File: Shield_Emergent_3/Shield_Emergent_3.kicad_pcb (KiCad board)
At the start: 2 copper layers, 23.6 x 33.4 mm, 17 parts, among them J1 USB3_B_Micro, J2 Conn_02x03_Odd_Even, J3 USB3_B_Micro, U3 SP3012-06UTG, U4 SP3012-06UTG, X1 USB_C_24pins

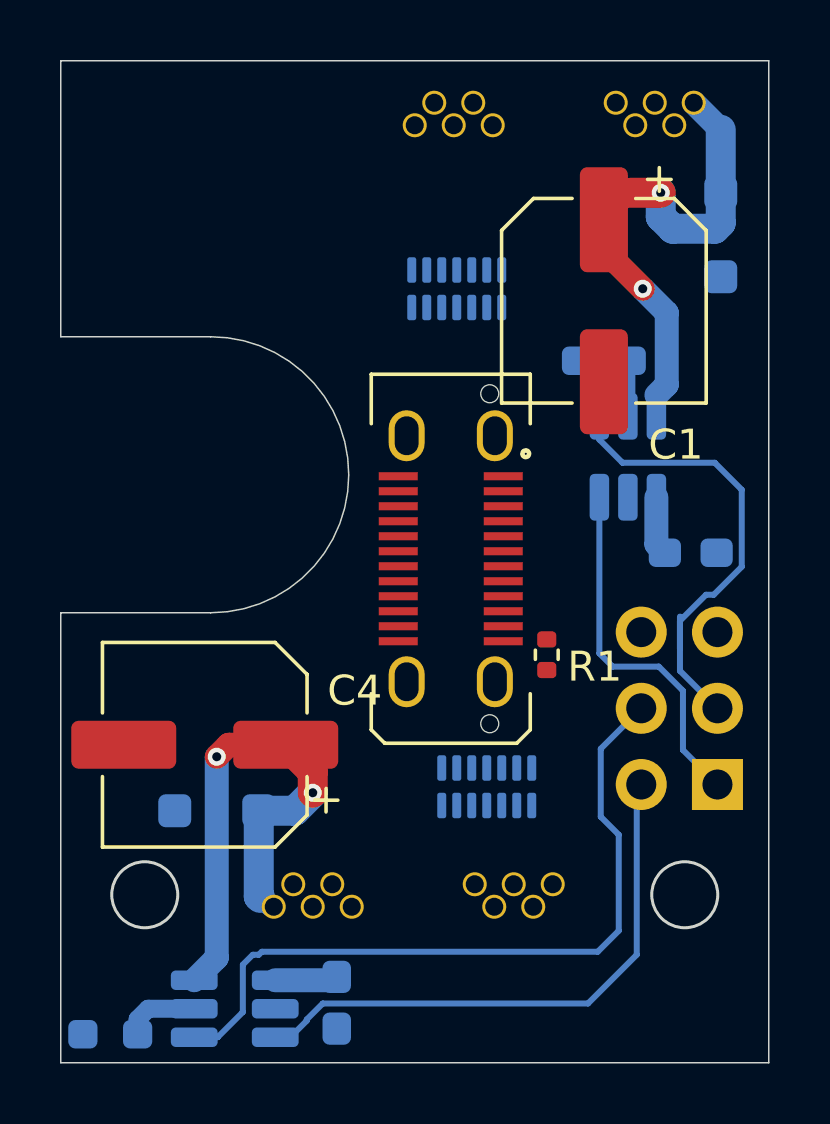
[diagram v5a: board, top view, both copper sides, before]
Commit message: v1.2 internal layers were added
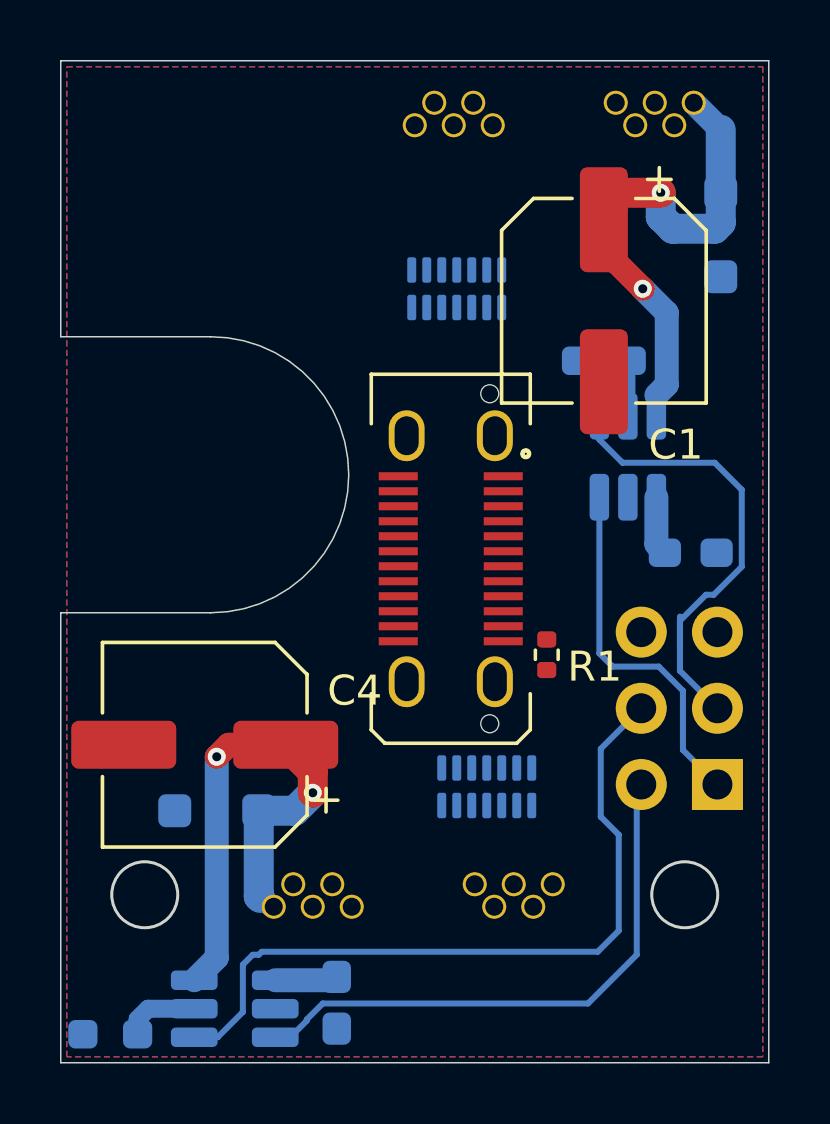
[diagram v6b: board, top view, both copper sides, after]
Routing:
- added copper zone on B.Cu, net GND
- added copper zone on F.Cu, net GND
- added copper zone on In1.Cu, net GND
- added copper zone on In2.Cu, net GND
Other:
- copper layers 2 -> 4
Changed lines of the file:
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@@
 	(layers
 		(0 "F.Cu" signal)
+		(1 "In1.Cu" signal)
+		(2 "In2.Cu" signal)
 		(31 "B.Cu" signal)
 		(32 "B.Adhes" user "B.Adhesive")
@@
 	)
 	(setup
+		(stackup
+			(layer "F.SilkS"
+				(type "Top Silk Screen")
+			)
+			(layer "F.Paste"
+				(type "Top Solder Paste")
+			)
+			(layer "F.Mask"
+				(type "Top Solder Mask")
+				(thickness 0.01)
+			)
+			(layer "F.Cu"
+				(type "copper")
+				(thickness 0.035)
+			)
+			(layer "dielectric 1"
+				(type "prepreg")
+				(thickness 0.1)
+				(material "FR4")
+				(epsilon_r 4.5)
+				(loss_tangent 0.02)
+			)
+			(layer "In1.Cu"
+				(type "copper")
+				(thickness 0.035)
+			)
+			(layer "dielectric 2"
+				(type "core")
+				(thickness 1.24)
+				(material "FR4")
+				(epsilon_r 4.5)
+				(loss_tangent 0.02)
+			)
+			(layer "In2.Cu"
+				(type "copper")
+				(thickness 0.035)
+			)
+			(layer "dielectric 3"
+				(type "prepreg")
+				(thickness 0.1)
+				(material "FR4")
+				(epsilon_r 4.5)
+				(loss_tangent 0.02)
+			)
+			(layer "B.Cu"
+				(type "copper")
+				(thickness 0.035)
+			)
+			(layer "B.Mask"
+				(type "Bottom Solder Mask")
+				(thickness 0.01)
+			)
+			(layer "B.Paste"
+				(type "Bottom Solder Paste")
+			)
+			(layer "B.SilkS"
+				(type "Bottom Silk Screen")
+			)
+			(copper_finish "None")
+			(dielectric_constraints no)
+		)
 		(pad_to_mask_clearance 0)
 		(allow_soldermask_bridges_in_footprints no)
@@
 		(net 27)
 	)
+	(zone
+		(net 2)
+		(net_name "GND")
+		(layers "F.Cu" "In1.Cu" "In2.Cu" "B.Cu")
+		(hatch edge 0.5)
+		(connect_pads
+			(clearance 0.5)
+		)
+		(min_thickness 0.25)
+		(filled_areas_thickness no)
+		(fill yes
+			(thermal_gap 0.5)
+			(thermal_bridge_width 0.5)
+		)
+		(polygon
+			(pts
+				(xy 2.4 0.4) (xy 25.6 0.4) (xy 25.6 33.4) (xy 2.4 33.4)
+			)
+		)
+	)
 )

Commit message: v1.3 draft routing was completed
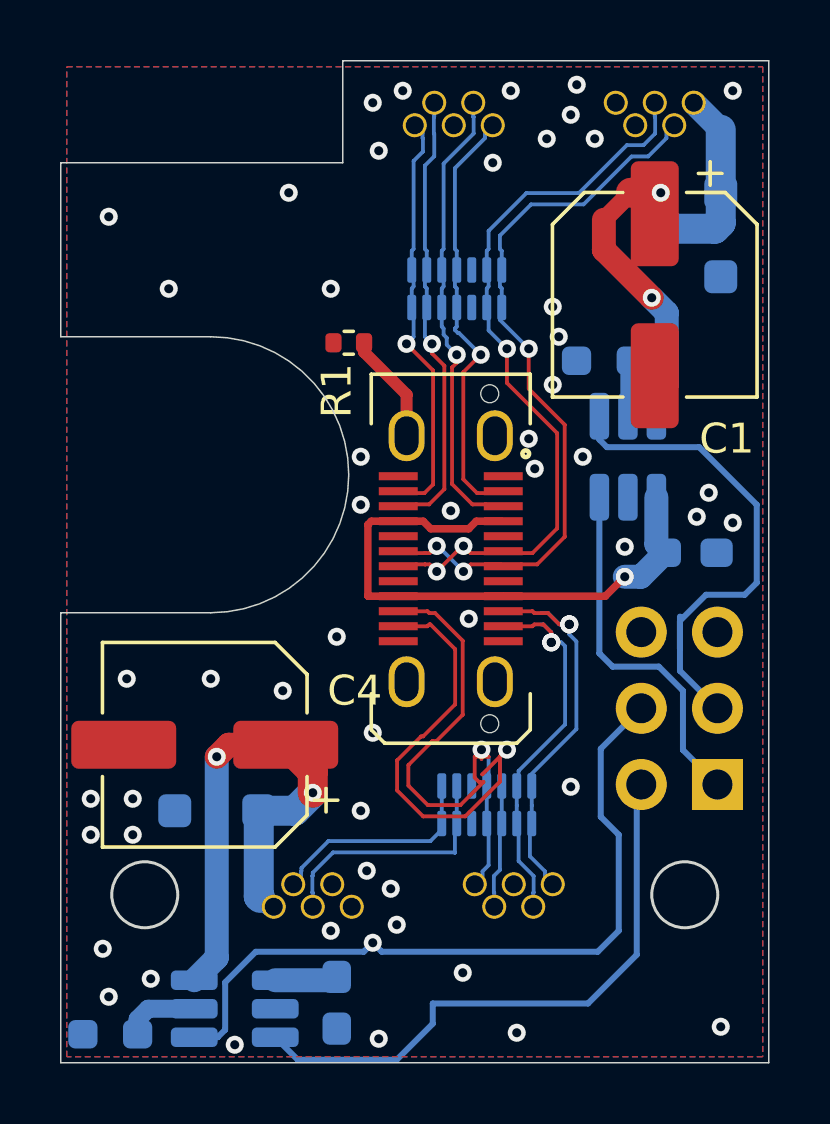
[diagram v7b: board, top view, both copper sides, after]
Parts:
- moved R1 12.3 mm to (11.8, 9.60), turned to 180 degrees
- moved C1 1.71 mm to (22.0, 8.00)
- moved U4 0.60 mm to (16.4, 25.0)
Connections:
- X1 pad A10: RX2- -> RX2+
- X1 pad A11: RX2+ -> RX2-
- X1 pad A2: TX1+ -> TX1-
- X1 pad A3: TX1- -> TX1+
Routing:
- net D-: track 0.00 -> 25.2 mm, vias 0 -> 3
- net D+: track 0.00 -> 25.2 mm, vias 0 -> 3
- net TX2-: track 0.00 -> 20.0 mm, vias 0 -> 1
- net TX2+: track 0.00 -> 18.6 mm, vias 0 -> 1
- net VBUS: track 4.06 -> 21.7 mm, vias 0 -> 1
- net TX1+: track 0.00 -> 15.5 mm, vias 0 -> 1
- net RX1-: track 0.00 -> 15.2 mm, vias 0 -> 1
- net TX1-: track 0.00 -> 14.7 mm, vias 0 -> 1
- net RX1+: track 0.00 -> 14.1 mm, vias 0 -> 1
- net RX2+: track 0.00 -> 14.0 mm, vias 0 -> 2
- net RX2-: track 0.00 -> 13.5 mm, vias 0 -> 2
- net 2_D+: track 0.00 -> 8.49 mm
- net 2_D-: track 0.00 -> 7.44 mm
- net Shield: track 0.00 -> 3.69 mm
- net nFLT1: track 16.1 -> 17.1 mm
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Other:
- outline, holes or cut-outs redrawn

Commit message: v1.4  draft ruting was totally completed.
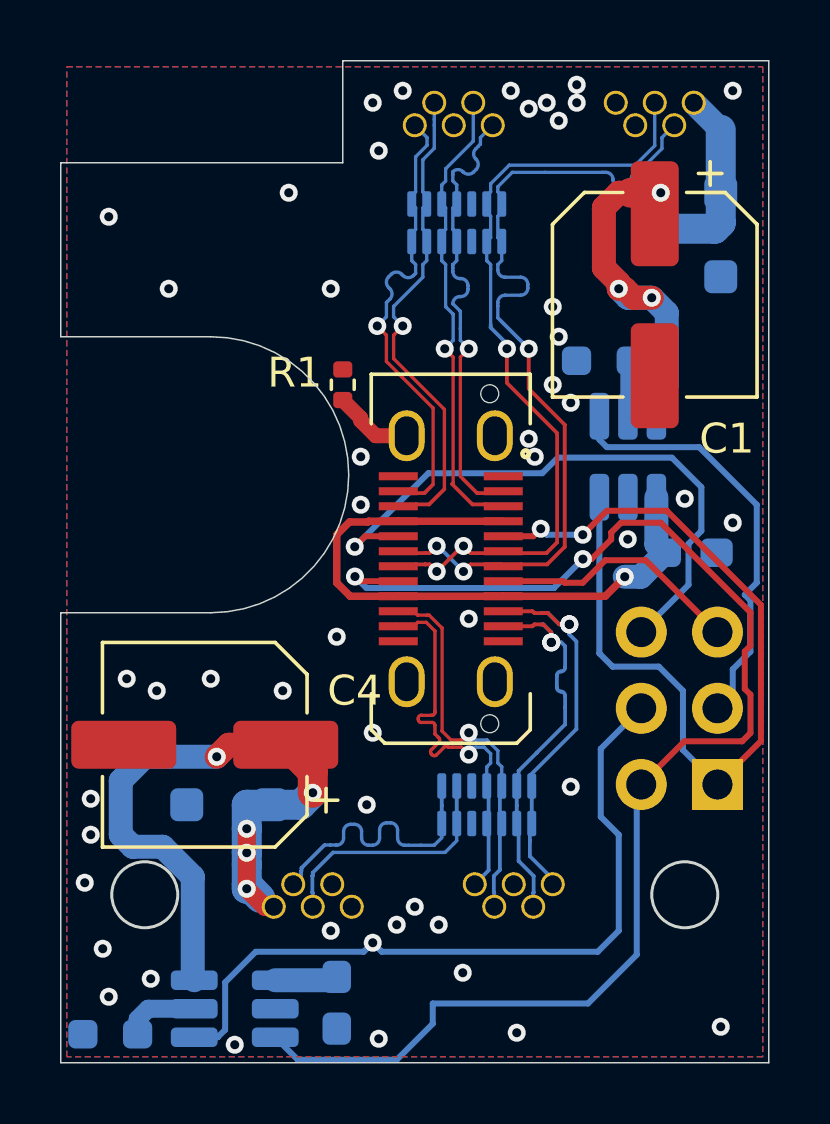
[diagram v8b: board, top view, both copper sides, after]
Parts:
- moved U3 2.20 mm to (15.4, 5.60)
- moved R1 1.41 mm to (11.6, 11.0), turned to 90 degrees
- moved D2 0.45 mm to (7.80, 25.0)
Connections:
- X1 pad A5: unconnected-(X1-CC1-PadA5) -> EN1
- X1 pad A8: unconnected-(X1-SBU1-PadA8) -> BTN1
- X1 pad B2: TX2- -> TX2+
- X1 pad B3: TX2+ -> TX2-
- X1 pad B5: unconnected-(X1-CC2-PadB5) -> EN2
- X1 pad B8: unconnected-(X1-SBU2-PadB8) -> BTN2
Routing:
- net EN2: track 19.9 -> 45.6 mm, vias 0 -> 2
- net BTN2: track 0.00 -> 20.4 mm, vias 0 -> 1
- net EN1: track 12.1 -> 29.1 mm, vias 0 -> 2
- net VOUT2: track 17.8 -> 26.9 mm, vias 2 -> 5
- net BTN1: track 0.00 -> 8.46 mm
- net TX2-: track 20.0 -> 13.4 mm
- net TX2+: track 18.6 -> 14.3 mm
- net D-: track 25.2 -> 28.6 mm
- net nFLT1: track 17.1 -> 14.4 mm
- net 2_D-: track 7.44 -> 9.72 mm
- net VOUT1: track 17.3 -> 19.2 mm, vias 2 -> 3
- net RX1+: track 14.1 -> 15.8 mm
- net D+: track 25.2 -> 26.6 mm
- net VBUS: track 21.7 -> 23.1 mm
- net RX1-: track 15.2 -> 16.4 mm
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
